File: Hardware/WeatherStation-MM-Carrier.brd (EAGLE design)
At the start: 67.3 x 58.4 mm, 152 parts, among them J11 microSD, J13 RJ11 - WIND, J15 MICROMOD-2222-C, J2 JTAG, J3 QWIIC_RIGHT_ANGLE, J7 RJ11 - RAIN, U1 BME280, U2 VEML6075, U3 AS3935, U5 AP7361C-33FGE

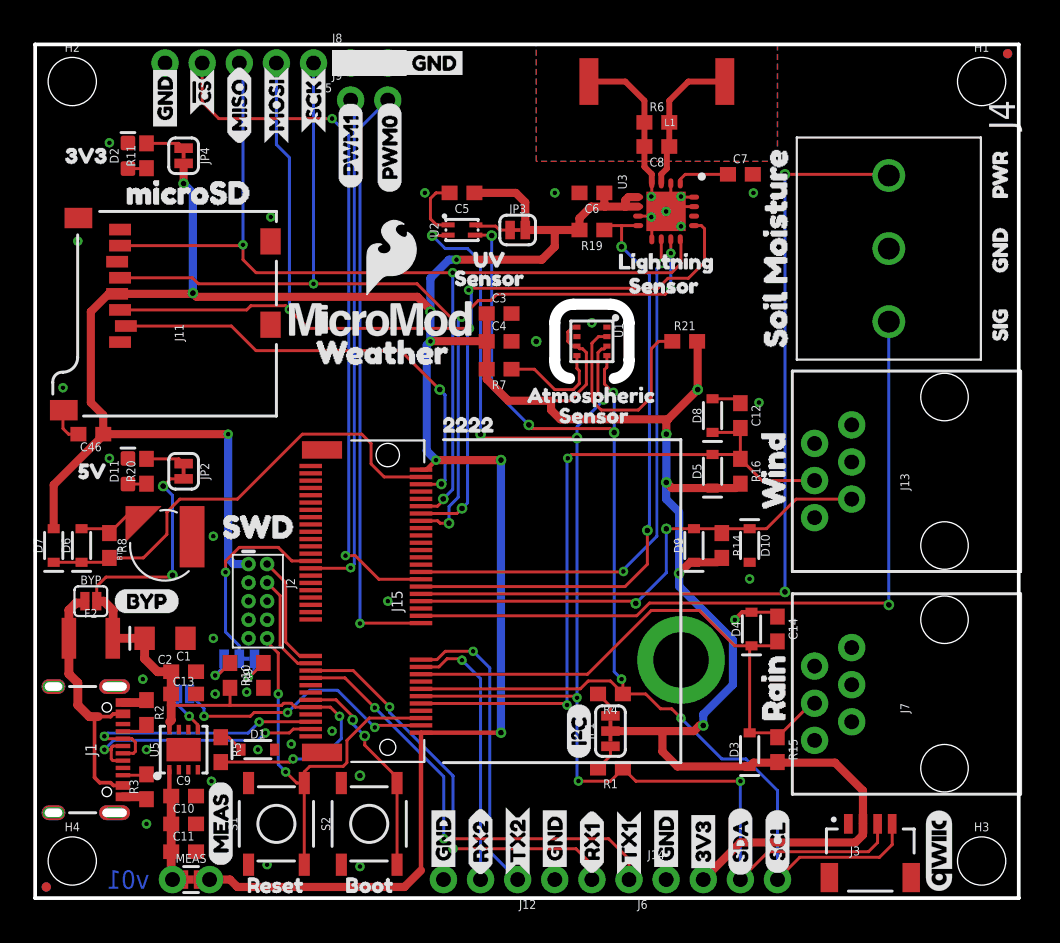
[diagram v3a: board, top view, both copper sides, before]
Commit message: Changes from Nate
Rotate soil moisture connector pins
MOSI/MISO --> COPI, POCI
Rotate LEDs
+/- silk on batt
Changed labels on jumpers
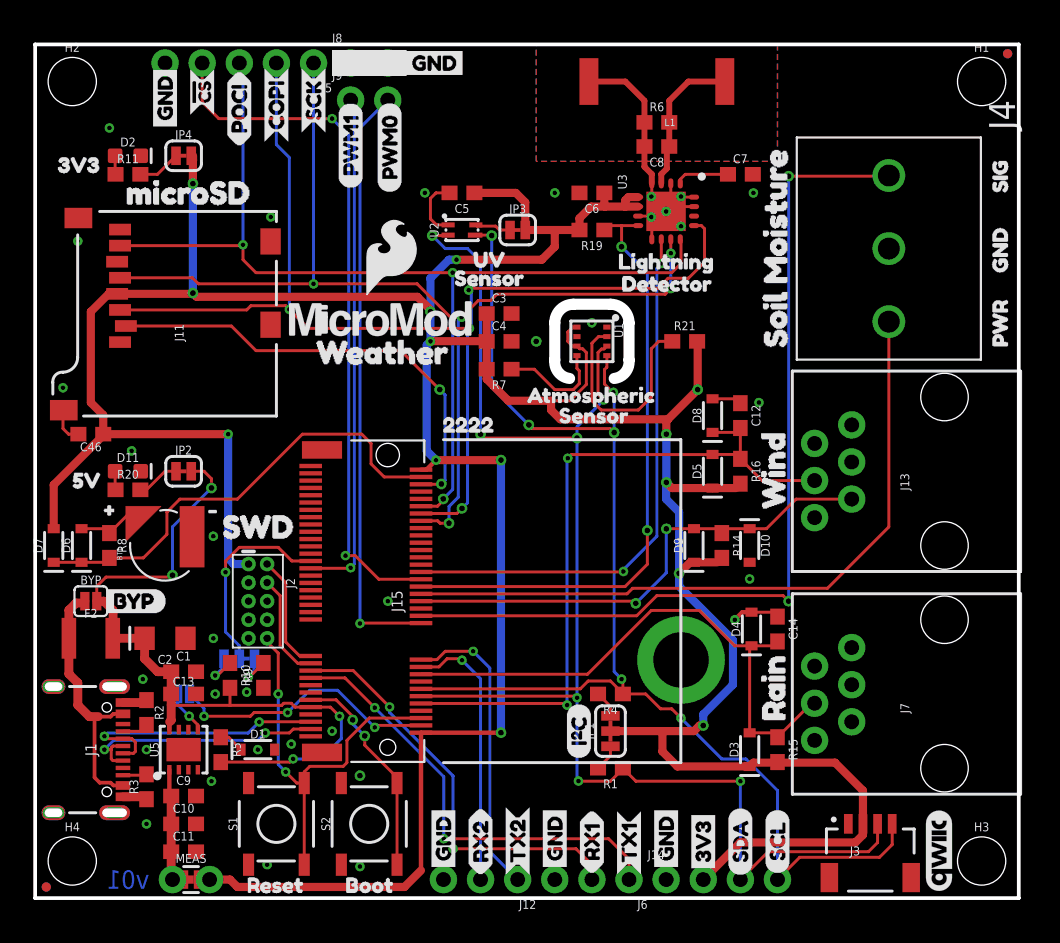
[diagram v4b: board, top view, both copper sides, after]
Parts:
- removed U$27: (no value), SparkFun-Buzzard:BYP
- added U$24: (no value), buzzard_labels (3):PWR2
- added U$57: (no value), buzzard_labels (3):GND0
- added U$63: (no value), buzzard_labels (3):SIG1
- added U$69: (no value), buzzard_labels (10):#0
- added U$70: (no value), buzzard_labels (10):#1
- added U$71: (no value), buzzard_labels (10):DETECTOR2
- U$14: device buzzard_labels (8):3#3V_EN0 -> buzzard_labels (11):BYP0
- U$21: device buzzard_labels (6):VIN#30 -> buzzard_labels (11):3#3V_EN2
- U$26: device buzzard_labels:SENSOR7 -> buzzard_labels (11):VIN#31
- U$50: device SparkFun-Buzzard:MOSI_O -> buzzard_labels (9):POCI1
- U$51: device SparkFun-Buzzard:MISO_I -> buzzard_labels (9):POCI1
- U$7: device SparkFun-Buzzard:MOSI_O -> buzzard_labels (9):COPI0
- U$8: device SparkFun-Buzzard:MISO_I -> buzzard_labels (9):COPI0
- moved U$26 37.0 mm to (12.8, 16.4), flipped to the bottom
- moved U$12 10.2 mm to (66.0, 36.8)
- moved U$13 10.2 mm to (66.0, 47.4)
- moved U$14 7.47 mm to (4.45, 20.3), flipped to the top
- moved LOGO3 4.43 mm to (3.68, 7.11)
- moved U$21 3.28 mm to (9.53, 13.8)
- moved U$50 2.54 mm to (14.0, 51.4), flipped to the top
- moved U$8 2.54 mm to (16.5, 51.6), flipped to the bottom
- moved R20 1.80 mm to (6.35, 27.9), turned to 0 degrees
- moved R11 1.80 mm to (6.35, 49.5), turned to 0 degrees
- moved U$5 1.76 mm to (13.6, 3.68), flipped to the bottom, turned to 0 degrees
- moved U$1 0.81 mm to (0.64, 50.2)
- moved U$18 0.74 mm to (1.65, 28.6)
- moved U$7 0.13 mm to (16.5, 51.7)
- moved U$51 0.13 mm to (14.0, 51.4)
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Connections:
- net SOIL_MOIST_PWR: now also J4.3; no longer J4.1
- net SOIL_MOIST_SIG: now also J4.1; no longer J4.3
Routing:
- net SOIL_MOIST_PWR: track 60.8 -> 48.0 mm, vias 2 -> 0
- net SOIL_MOIST_SIG: track 51.8 -> 61.8 mm, vias 1 -> 2
- net VIN: track 51.3 -> 52.7 mm

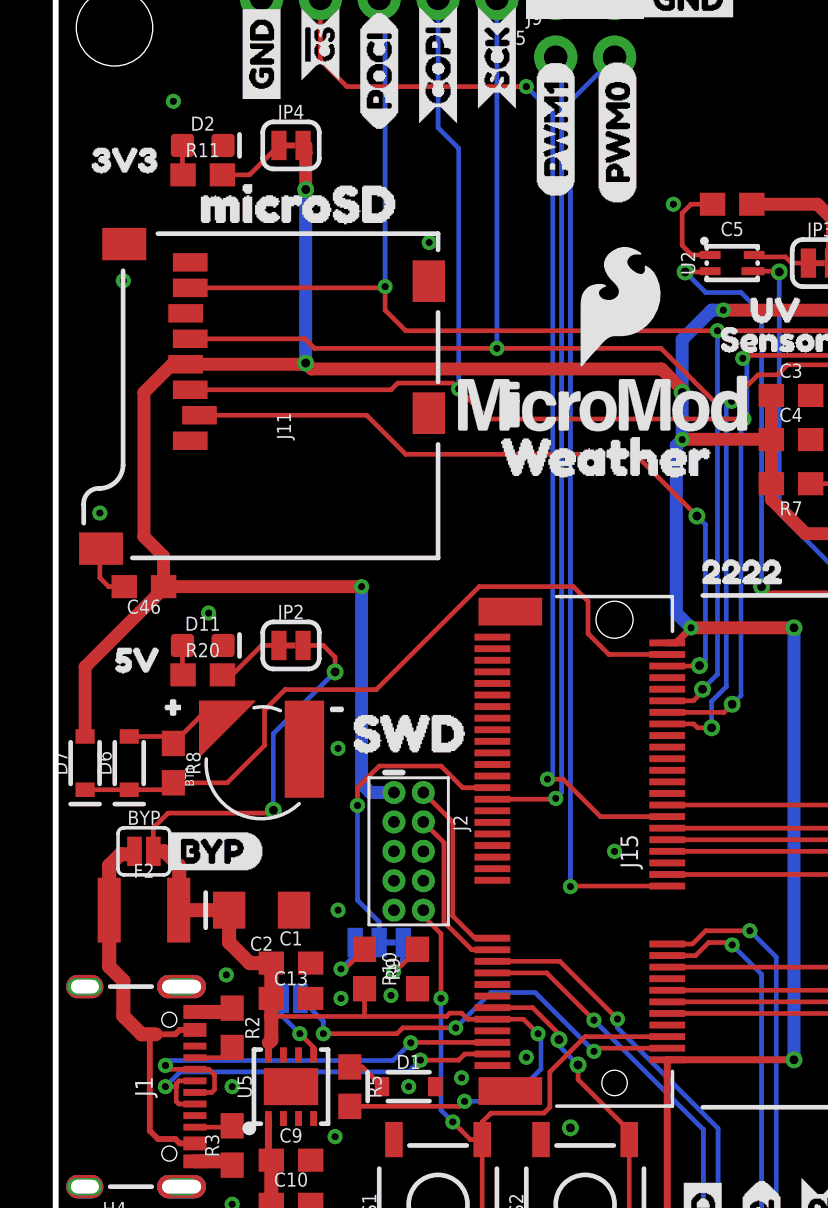
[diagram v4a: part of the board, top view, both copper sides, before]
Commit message: Added serial test. Updated brd to pass design rules
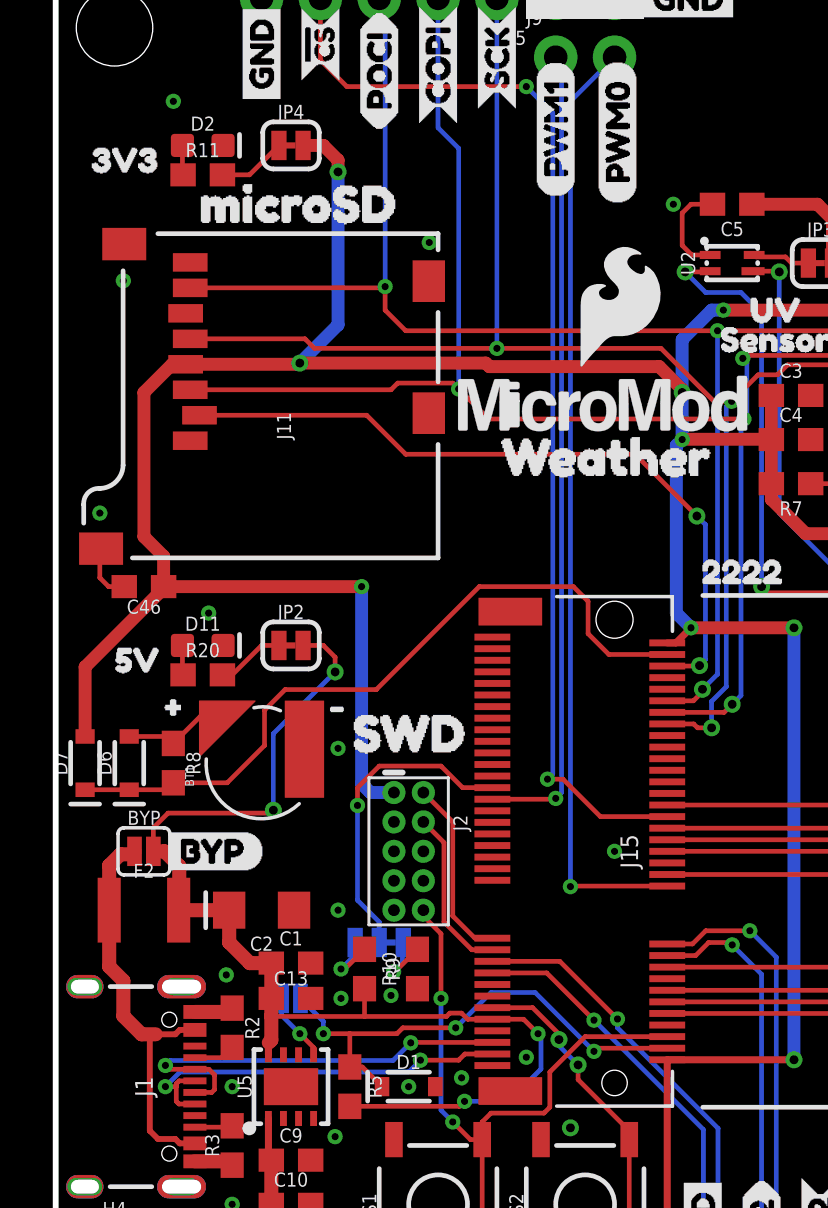
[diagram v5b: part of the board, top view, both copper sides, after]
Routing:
- net 3.3V: track 272.4 -> 274.2 mm
- net 3.3V_EN: track 23.4 -> 24.8 mm
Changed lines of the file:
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@@
 <drawing>
 <settings>
-<setting alwaysvectorfont="yes"/>
+<setting alwaysvectorfont="no"/>
 <setting verticaltext="up"/>
 </settings>
@@
 <wire x1="4.738" y1="31.75" x2="4.699" y2="31.711" width="0.2032" layer="1"/>
 <wire x1="4.66" y1="31.75" x2="4.699" y2="31.789" width="0.5588" layer="1"/>
-<wire x1="5.08" y1="41.402" x2="5.558" y2="41.402" width="0.5588" layer="1"/>
-<wire x1="5.558" y1="41.402" x2="5.61" y2="41.35" width="0.2032" layer="1"/>
-<wire x1="5.61" y1="41.35" x2="10.743" y2="41.35" width="0.5588" layer="1"/>
-<wire x1="10.743" y1="41.35" x2="10.795" y2="41.402" width="0.2032" layer="1"/>
-<via x="10.795" y="41.402" extent="1-16" drill="0.381"/>
 <wire x1="39.26" y1="11.32" x2="39.37" y2="11.43" width="0.2032" layer="1"/>
 <wire x1="41.2634" y1="47.3216" x2="40.386" y2="47.3216" width="0.5588" layer="1"/>
@@
 <wire x1="40.386" y1="47.752" x2="40.386" y2="47.3216" width="0.5588" layer="1"/>
 <wire x1="40.6056" y1="47.9716" x2="40.386" y2="47.752" width="0.5588" layer="1"/>
-<wire x1="11.049" y1="41.148" x2="26.162" y2="41.148" width="0.5588" layer="1"/>
-<wire x1="10.795" y1="41.402" x2="11.049" y2="41.148" width="0.5588" layer="1"/>
 <wire x1="37.25" y1="45.72" x2="37.25" y2="46.521" width="0.5588" layer="1"/>
 <wire x1="38.0506" y1="47.3216" x2="38.989" y2="47.3216" width="0.5588" layer="1"/>
@@
 <wire x1="38.95" y1="48.26" x2="38.95" y2="47.3606" width="0.5588" layer="1"/>
 <wire x1="38.95" y1="47.3606" x2="38.989" y2="47.3216" width="0.2032" layer="1"/>
-<via x="10.795" y="48.895" extent="1-16" drill="0.381"/>
-<wire x1="10.795" y1="48.895" x2="10.795" y2="41.402" width="0.5588" layer="16"/>
-<wire x1="26.162" y1="41.148" x2="27.051" y2="40.259" width="0.5588" layer="1"/>
 <wire x1="27.051" y1="40.259" x2="27.051" y2="40.132" width="0.5588" layer="1"/>
 <via x="27.051" y="40.132" extent="1-16" drill="0.381"/>
@@
 <wire x1="4.66" y1="33.059" x2="3.81" y2="33.909" width="0.5588" layer="1"/>
 <wire x1="3.81" y1="33.909" x2="3.81" y2="40.132" width="0.5588" layer="1"/>
-<wire x1="3.81" y1="40.132" x2="5.08" y2="41.402" width="0.5588" layer="1"/>
 <wire x1="33.5407" y1="45.72" x2="35.56" y2="45.72" width="0.5588" layer="1"/>
 <wire x1="35.56" y1="45.72" x2="37.211" y2="45.72" width="0.5588" layer="1"/>
@@
 <wire x1="48.895" y1="9.01" x2="43.949" y2="9.01" width="0.5588" layer="1"/>
 <wire x1="43.949" y1="9.01" x2="42.926" y2="10.033" width="0.5588" layer="1"/>
-<wire x1="10.795" y1="48.895" x2="10.795" y2="50.4682875" width="0.5588" layer="1"/>
-<wire x1="10.795" y1="50.4682875" x2="10.8077" y2="50.4809875" width="0.5588" layer="1"/>
-<wire x1="10.8077" y1="50.4809875" x2="10.8077" y2="50.8" width="0.5588" layer="1"/>
-<wire x1="10.8077" y1="50.8" x2="10.6807" y2="50.8" width="0" layer="19" extent="1-1"/>
+<wire x1="10.6807" y1="50.8" x2="11.557" y2="50.8" width="0.5588" layer="1"/>
+<wire x1="12.192" y1="50.165" x2="12.192" y2="49.657" width="0.5588" layer="1"/>
+<via x="12.192" y="49.657" extent="1-16" drill="0.381"/>
+<wire x1="12.192" y1="49.657" x2="12.192" y2="43.053" width="0.5588" layer="16"/>
+<wire x1="12.192" y1="43.053" x2="10.541" y2="41.402" width="0.5588" layer="16"/>
+<via x="10.541" y="41.402" extent="1-16" drill="0.381"/>
+<wire x1="11.557" y1="50.8" x2="12.192" y2="50.165" width="0.5588" layer="1"/>
+<wire x1="10.541" y1="41.402" x2="18.57144375" y2="41.402" width="0.5588" layer="1"/>
+<wire x1="18.57144375" y1="41.402" x2="18.72384375" y2="41.2496" width="0.5588" layer="1"/>
+<wire x1="18.72384375" y1="41.2496" x2="26.0604" y2="41.2496" width="0.5588" layer="1"/>
+<wire x1="26.0604" y1="41.2496" x2="27.051" y2="40.259" width="0.5588" layer="1"/>
+<wire x1="3.81" y1="40.132" x2="5.028" y2="41.35" width="0.5588" layer="1"/>
+<wire x1="5.028" y1="41.35" x2="5.61" y2="41.35" width="0.5588" layer="1"/>
+<wire x1="5.61" y1="41.35" x2="10.489" y2="41.35" width="0.5588" layer="1"/>
+<wire x1="10.489" y1="41.35" x2="10.541" y2="41.402" width="0.5588" layer="1"/>
 </signal>
 <signal name="USB_D-">
@@
 <wire x1="10.5664" y1="13.97" x2="11.557" y2="12.9794" width="0.2032" layer="16"/>
 <via x="11.557" y="12.446" extent="1-16" drill="0.3048"/>
-<wire x1="11.557" y1="12.446" x2="14.732" y2="12.446" width="0.2032" layer="1"/>
+<wire x1="11.557" y1="12.446" x2="12.7" y2="12.446" width="0.2032" layer="1"/>
+<wire x1="12.7" y1="12.446" x2="14.732" y2="12.446" width="0.2032" layer="1"/>
 <wire x1="14.986" y1="12.7" x2="14.732" y2="12.446" width="0.2032" layer="1"/>
 <wire x1="14.986" y1="12.7" x2="17.272" y2="12.7" width="0.2032" layer="1"/>
 <wire x1="11.557" y1="12.9794" x2="11.557" y2="12.446" width="0.2032" layer="16"/>
-<wire x1="11.135" y1="11.535" x2="12.7" y2="11.01" width="0" layer="19" extent="1-1"/>
+<wire x1="12.7" y1="11.01" x2="12.7" y2="12.446" width="0.2032" layer="1"/>
 <wire x1="10.5664" y1="13.97" x2="9.7536" y2="13.97" width="0" layer="19" extent="16-16"/>
 </signal>

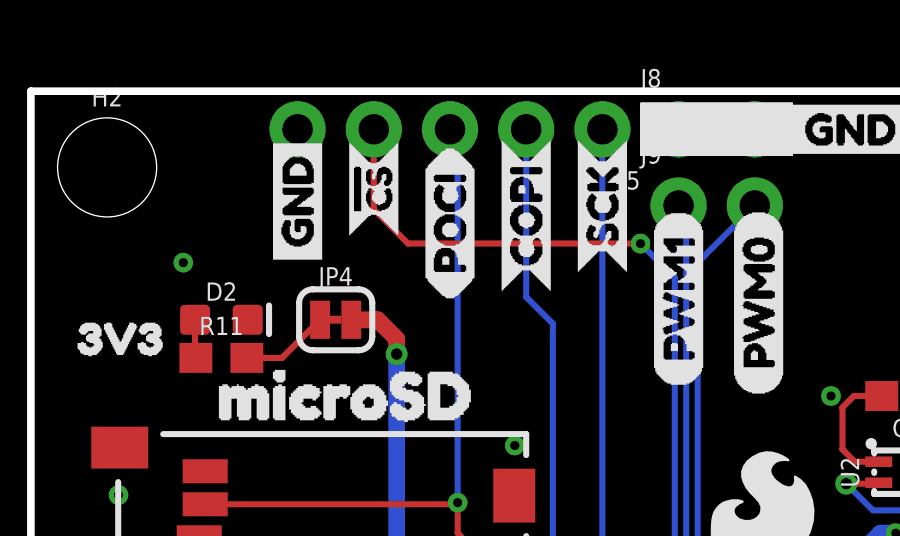
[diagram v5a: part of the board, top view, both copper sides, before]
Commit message: Changed "POCI" label to "CIPO"
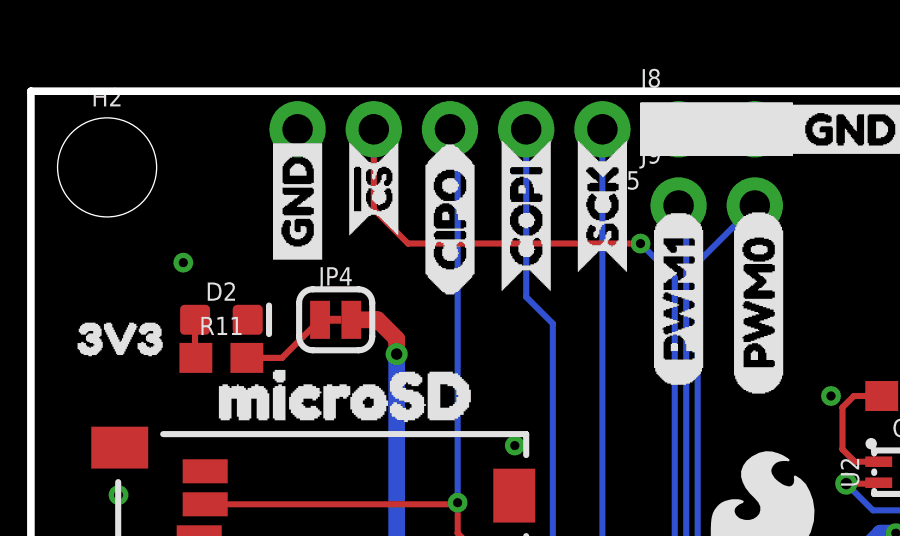
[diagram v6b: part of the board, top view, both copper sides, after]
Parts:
- removed U$51: (no value), buzzard_labels (9):POCI1
- added U$27: (no value), buzzard_labels (12):CIPO0
- U$50: device buzzard_labels (9):POCI1 -> buzzard_labels (12):CIPO0
- moved U$50 0.13 mm to (14.0, 51.6), flipped to the bottom
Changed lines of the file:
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@@
 <drawing>
 <settings>
-<setting alwaysvectorfont="no"/>
+<setting alwaysvectorfont="yes"/>
 <setting verticaltext="up"/>
 </settings>
@@
 <element name="U$7" library="buzzard_labels (9)" package="COPI0" value="" x="16.51" y="51.689" smashed="yes" rot="R90"/>
 <element name="U$8" library="buzzard_labels (9)" package="COPI0" value="" x="16.51" y="51.562" smashed="yes" rot="MR90"/>
-<element name="U$50" library="buzzard_labels (9)" package="POCI1" value="" x="13.97" y="51.435" smashed="yes" rot="R90"/>
-<element name="U$51" library="buzzard_labels (9)" package="POCI1" value="" x="13.97" y="51.435" smashed="yes" rot="MR90"/>
 <element name="U$69" library="buzzard_labels (10)" package="#0" value="" x="3.81" y="26.67" smashed="yes"/>
 <element name="U$70" library="buzzard_labels (10)" package="#1" value="" x="10.922" y="26.67" smashed="yes"/>
@@
 <element name="U$21" library="buzzard_labels (11)" package="3#3V_EN2" value="" x="9.525" y="13.843" smashed="yes" rot="MR0"/>
 <element name="U$26" library="buzzard_labels (11)" package="VIN#31" value="" x="12.827" y="16.383" smashed="yes" rot="MR0"/>
+<element name="U$27" library="buzzard_labels (12)" package="CIPO0" value="" x="13.97" y="51.562" smashed="yes" rot="R90"/>
+<element name="U$50" library="buzzard_labels (12)" package="CIPO0" value="" x="13.97" y="51.562" smashed="yes" rot="MR90"/>
 </elements>
 <signals>
